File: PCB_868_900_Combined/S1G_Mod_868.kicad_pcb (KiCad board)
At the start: 4 copper layers, 60 x 27 mm, 89 parts, among them J2 20021121-00010C4LF, J5 0475890001-MicroUSBPort, P1 61301621121, Q1 DMG2307L-7, SW1 CUS-12TB, SW2 B3U-1000P, T1 0732511150, U1 AP7361-33FGE-7, U2 ADF7023BCPZ, U3 STM32L052C8T6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

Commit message: Readme
Readme updated and boms exported.
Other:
- board text added: "PWR"
- board text removed: "CERN OSHWL 1.2 Nov 2016"
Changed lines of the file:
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@@
     (links 234)
     (no_connects 0)
-    (area 39.924999 33.1276 120.075001 67.3654)
+    (area 56.424999 37.924999 116.575001 65.075001)
     (thickness 1.6)
     (drawings 15)
@@
   (layers
     (0 F.Cu signal)
-    (1 In1.Cu power hide)
-    (2 In2.Cu power hide)
-    (31 B.Cu signal hide)
+    (1 In1.Cu power)
+    (2 In2.Cu power)
+    (31 B.Cu signal)
     (32 B.Adhes user)
     (33 F.Adhes user)
@@
     (38 B.Mask user)
     (39 F.Mask user)
-    (40 Dwgs.User user)
+    (40 Dwgs.User user hide)
     (41 Cmts.User user)
     (42 Eco1.User user)
@@
       (drillshape 0)
       (scaleselection 1)
-      (outputdirectory ""))
+      (outputdirectory Fab_Outputs/))
   )
   (net 0 "")
@@
   (module PCB_Footprints:LED0603 (layer F.Cu)
     (at 105.425 50.6 180)
-    (fp_text reference LED4 (at -0.375 0.9 180) (layer F.SilkS)
+    (fp_text reference LED4 (at 1.675 -1.05 180) (layer F.SilkS)
       (effects (font (size 0.5 0.5) (thickness 0.1)))
     )
@@
     )
   )
+  (gr_text PWR (at 103.85 49.35) (layer F.SilkS)
+    (effects (font (size 1 1) (thickness 0.15)) (justify left))
+  )
   (gr_text RST (at 86.8 45.3 90) (layer F.SilkS)
     (effects (font (size 1 1) (thickness 0.15)) (justify left))
@@
     (effects (font (size 1 1) (thickness 0.18)) (justify left mirror))
   )
-  (gr_text "CERN OSHWL 1.2 Nov 2016" (at 61.9 63.6) (layer F.SilkS)
-    (effects (font (size 1 1) (thickness 0.15)) (justify left))
-  )
   (gr_line (start 40 51.5) (end 120 51.5) (layer Dwgs.User) (width 0.15))
   (gr_text "S1G-RF 01.a - 915MHZ Radio\n" (at 62.3 39.6) (layer F.SilkS)
@@
   (segment (start 99.14 49.75) (end 100.85 49.75) (width 0.1778) (layer F.Cu) (net 42))
   (segment (start 100.85 49.75) (end 101.3 49.3) (width 0.1778) (layer F.Cu) (net 42))
-  (segment (start 101.3 49.3) (end 101.3 44.4) (width 0.1778) (layer F.Cu) (net 42))
-  (segment (start 101.3 44.4) (end 100.94 44.04) (width 0.1778) (layer F.Cu) (net 42))
-  (segment (start 100.94 44.04) (end 99.33 44.04) (width 0.1778) (layer F.Cu) (net 42))
+  (segment (start 101.3 49.3) (end 101.3 44.5) (width 0.1778) (layer F.Cu) (net 42))
+  (segment (start 101.3 44.5) (end 100.84 44.04) (width 0.1778) (layer F.Cu) (net 42))
+  (segment (start 100.84 44.04) (end 99.33 44.04) (width 0.1778) (layer F.Cu) (net 42))
   (segment (start 99.53 44.04) (end 100.66 44.04) (width 0.1778) (layer F.Cu) (net 42))
   (segment (start 99.14 50.75) (end 101.99 50.75) (width 0.1778) (layer F.Cu) (net 44))
@@
   (segment (start 94.14 46.573) (end 93.55 45.983) (width 0.1778) (layer F.Cu) (net 54))
   (segment (start 93.54 45.993) (end 93.55 45.983) (width 0.1778) (layer F.Cu) (net 54))
-  (segment (start 99.33 42.77) (end 100.355 42.77) (width 0.1778) (layer F.Cu) (net 59))
-  (segment (start 100.355 42.77) (end 101.7 44.115) (width 0.1778) (layer F.Cu) (net 59))
-  (segment (start 101.7 44.115) (end 101.7 46.800012) (width 0.1778) (layer F.Cu) (net 59))
+  (segment (start 99.33 42.77) (end 100.22 42.77) (width 0.1778) (layer F.Cu) (net 59))
+  (segment (start 100.22 42.77) (end 101.7 44.25) (width 0.1778) (layer F.Cu) (net 59))
+  (segment (start 101.7 44.25) (end 101.7 46.800012) (width 0.1778) (layer F.Cu) (net 59))
   (segment (start 101.7 46.800012) (end 102.099988 47.2) (width 0.1778) (layer F.Cu) (net 59))
   (segment (start 98.3 47.2) (end 102.099988 47.2) (width 0.1778) (layer B.Cu) (net 59))

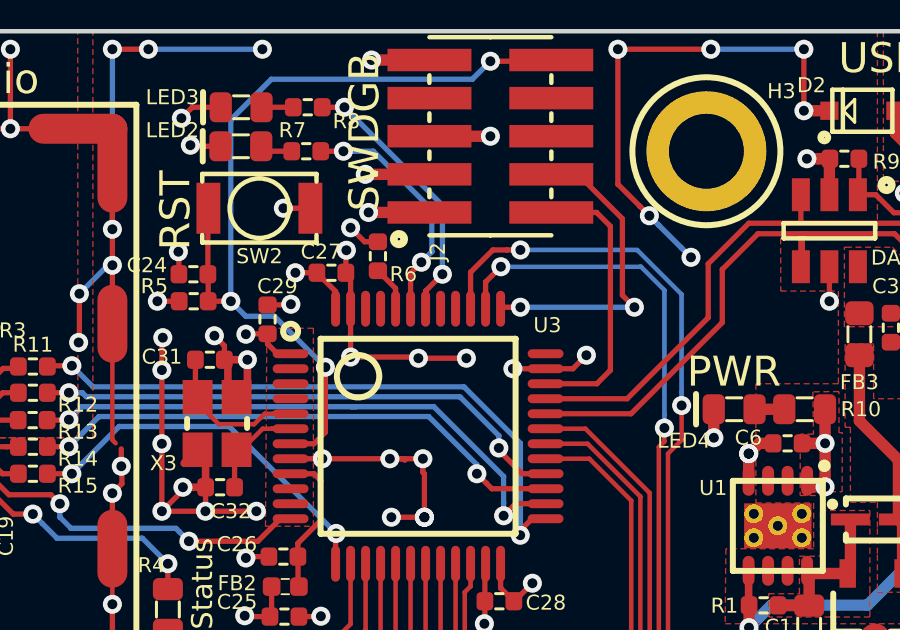
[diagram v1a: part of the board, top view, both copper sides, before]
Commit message: USB VDD
Found schematic bug, USB VDD was not tied to 3V3 supply or applied a
bypass cap, this has been resolved in both implementations of the S1G.
STM32L0 program manual added to the datasheets collection for the
project. Schematic PDFs updated.
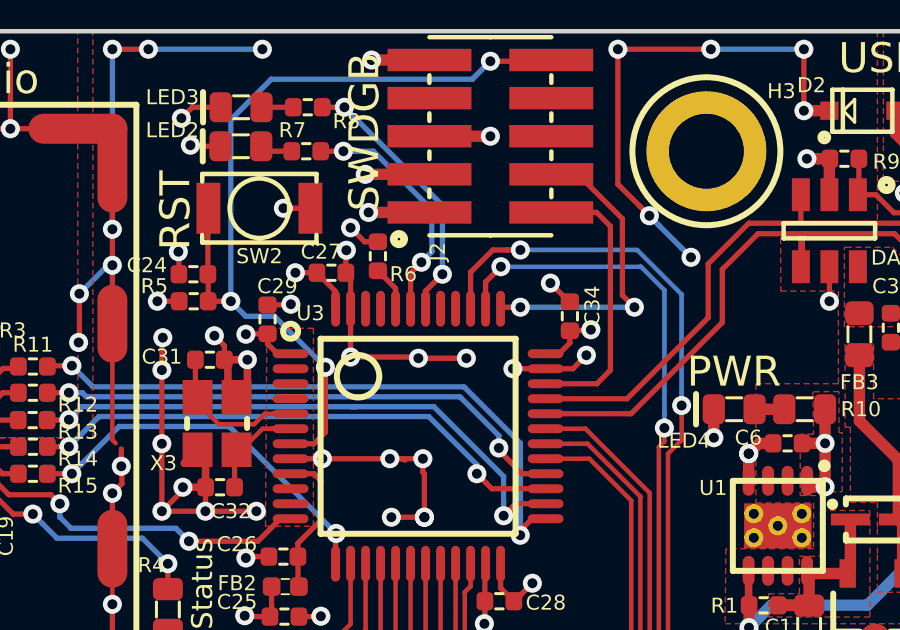
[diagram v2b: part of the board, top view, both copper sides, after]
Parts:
- added C34: CL05B104JP5NNNC, PCB_Footprints:C0402, F.Cu at (100.0, 47.5)
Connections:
- U3 pad 36: Net-(U3-Pad36) -> +3V3
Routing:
- net +3V3: track 24.3 -> 26.4 mm, vias 12 -> 13
- net GND: track 373.3 -> 374.2 mm, vias 174 -> 175

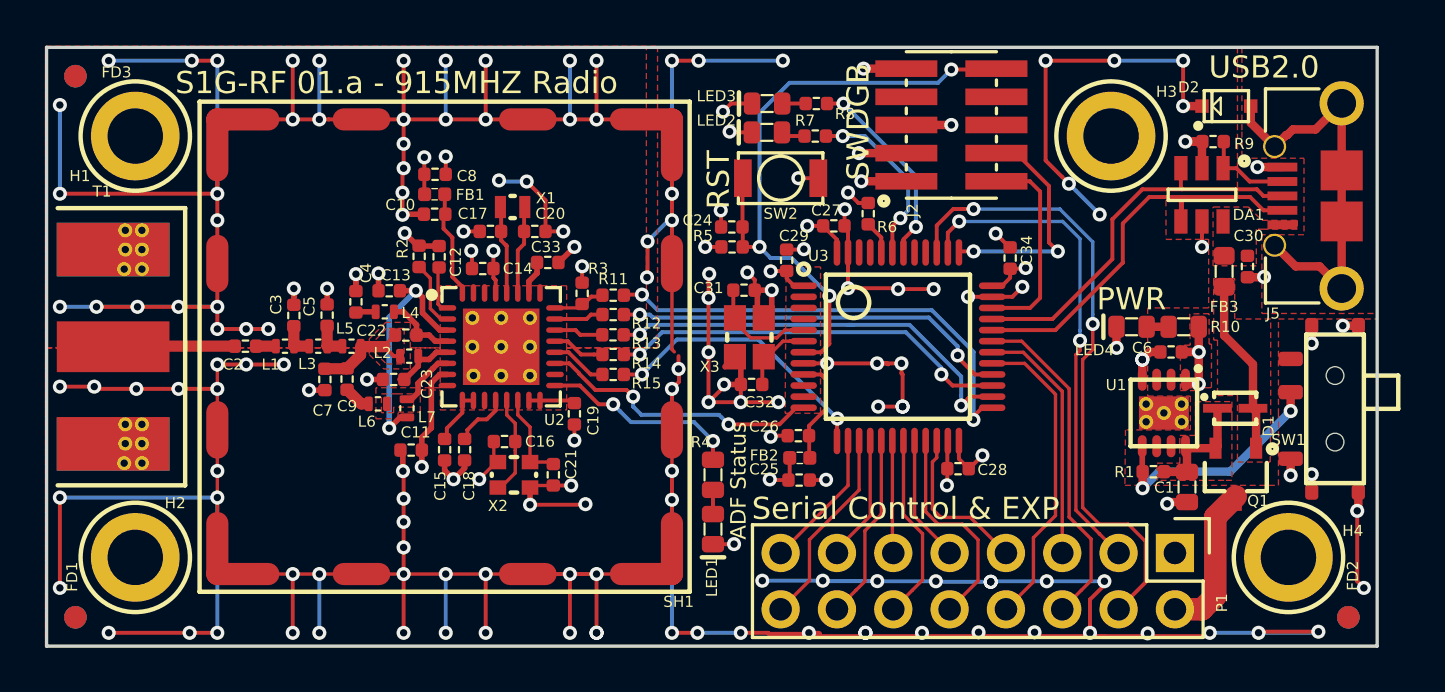
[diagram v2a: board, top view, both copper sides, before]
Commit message: 0.22uF cap
0.22uF cap replaced with 0402 part instead of the massive 0603 part.
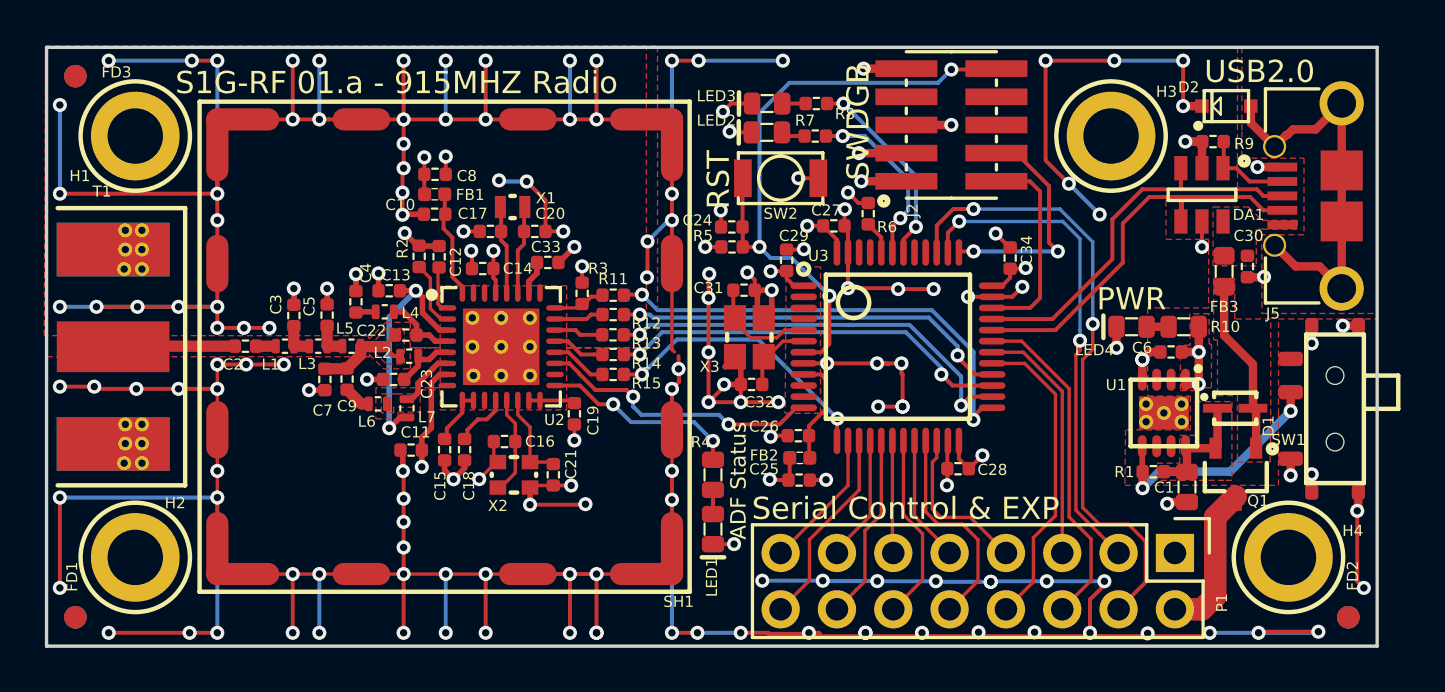
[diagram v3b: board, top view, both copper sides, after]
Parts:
- C12, C13, C15, C19, C33: value CL10B224JO8NNNC -> CL05A224KP5NNNC
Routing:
- net Net-(C22-Pad1): track 4.80 -> 5.95 mm

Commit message: Radio Reference Schematic Errors
Some errors transcribing ADI's reference shcematic. 0.22uF caps added to
pins that needed it etc.
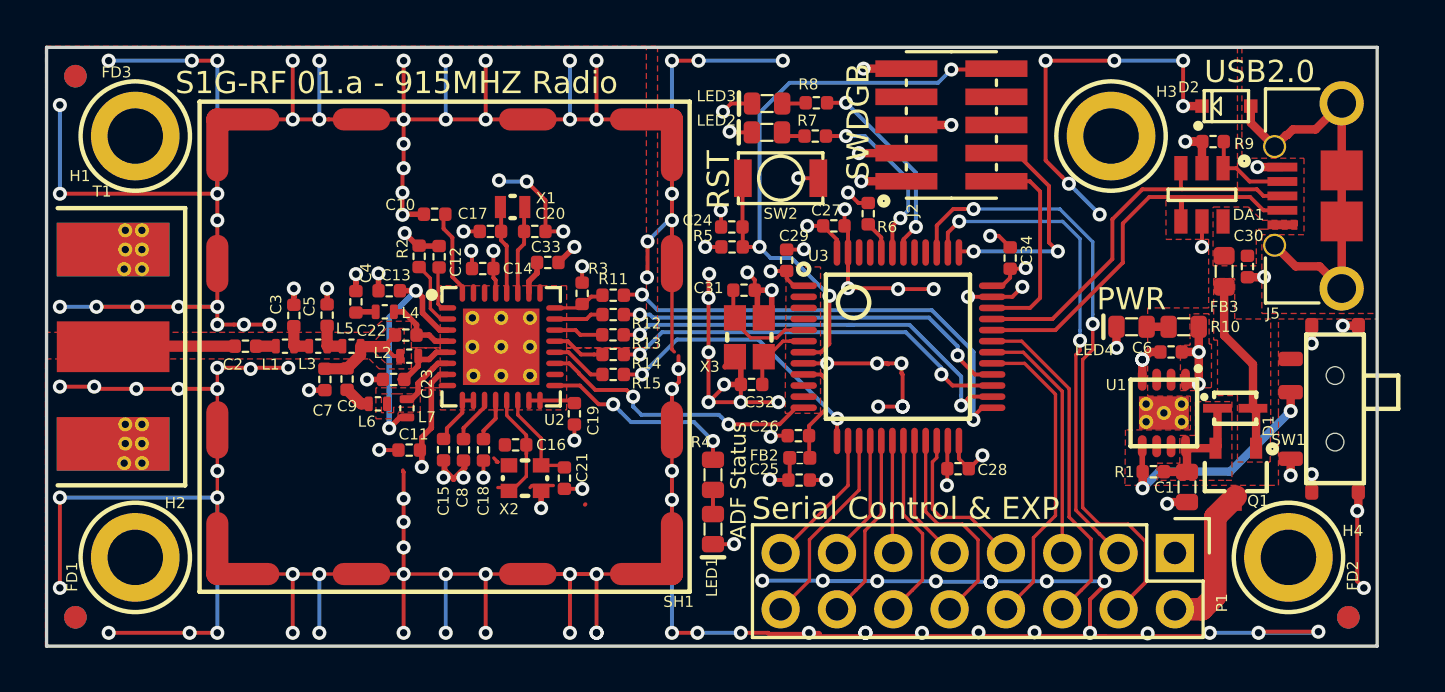
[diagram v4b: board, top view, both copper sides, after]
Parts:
- removed FB1: BLM15HG601SN1D, PCB_Footprints:BLM15HG601SN1D
- C10, C8: value CL05B104JP5NNNC -> CL05A224KP5NNNC
- moved C8 12.5 mm to (75.3, 56.1), turned to 270 degrees
- moved C18 0.85 mm to (76.2, 56.1)
- moved C16 0.52 mm to (77.7, 55.9)
- moved C21 0.52 mm to (79.8, 57.4)
- moved X2 0.52 mm to (78.1, 57.4)
- moved C11 0.09 mm to (72.8, 56.2)
- turned R8 to 180 degrees
- turned R7 to 180 degrees
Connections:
- net /VREF renamed Net-(C10-Pad2)
- C8 pad 1: GND -> Net-(C8-Pad1)
- C8 pad 2: +3V3 -> GND
- R7 pad 1: Net-(LED2-Pad1) -> /MCU - STM32L052K8T6/HB_2
- R7 pad 2: Net-(R7-Pad2) -> Net-(LED2-Pad1)
- R8 pad 1: Net-(LED3-Pad1) -> /MCU - STM32L052K8T6/HB_1
- R8 pad 2: Net-(R8-Pad2) -> Net-(LED3-Pad1)
- U2 pad 11: Net-(U2-Pad11) -> Net-(C8-Pad1)
- U3 pad 42: Net-(R8-Pad2) -> /MCU - STM32L052K8T6/HB_1
- U3 pad 43: Net-(R7-Pad2) -> /MCU - STM32L052K8T6/HB_2
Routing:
- net /MCU - STM32L052K8T6/HB_1: track 0.00 -> 9.14 mm, vias 0 -> 2
- net Net-(R8-Pad2): track 9.04 -> 0.00 mm, vias 2 -> 0
- net Net-(R7-Pad2): track 8.11 -> 0.00 mm, vias 2 -> 0
- net /MCU - STM32L052K8T6/HB_2: track 0.00 -> 8.11 mm, vias 0 -> 2
- net GND: track 374.4 -> 370.9 mm, vias 175 -> 174
- net Net-(C8-Pad1): track 0.00 -> 2.14 mm
- net +3V3: track 26.4 -> 24.7 mm, vias 13 -> 12
- net (no net): track 0.00 -> 1.45 mm
- net Net-(C10-Pad2): track 4.92 -> 3.98 mm

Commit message: PDF
schematic exported as color PDF for review
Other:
- board text added: "Hackaday Prize 2017 - adamjvr"
- board text added: "S1G RF 01.a - 915MHZ Radio CERN OSHW 1.2 July 2017 Designed by Adam Vadala-Roth https://github.com/adamjvr/S1G-Mod"
- board text removed: "S1G RF 01.a - 915MHZ Radio CERN OSHW 1.2 Nov 2016 Designed by Adam Vadala-Roth https://github.com/adamjvr/S1G-Mod"
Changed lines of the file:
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@@
     (area 39.924999 24.75 146.100001 67.3654)
     (thickness 1.6)
-    (drawings 17)
+    (drawings 18)
     (tracks 993)
     (zones 0)
@@
     (34 B.Paste user)
     (35 F.Paste user)
-    (36 B.SilkS user hide)
+    (36 B.SilkS user)
     (37 F.SilkS user)
     (38 B.Mask user)
@@
   (module PCB_Footprints:36103205 locked (layer F.Cu)
     (at 74.45 51.5)
-    (fp_text reference SH1 (at 10.55 11.5) (layer F.SilkS)
+    (fp_text reference SH1 (at -11.5 -7.55 90) (layer F.SilkS)
       (effects (font (size 0.5 0.5) (thickness 0.1)))
     )
@@
     )
   )
+  (gr_text "Hackaday Prize 2017 - adamjvr " (at 62.15 63.45) (layer F.SilkS)
+    (effects (font (size 1 1) (thickness 0.18)) (justify left))
+  )
   (dimension 60 (width 0.3) (layer Eco1.User)
     (gr_text "60.000 mm" (at 86.5 26.1) (layer Eco1.User)
@@
     (effects (font (size 1 1) (thickness 0.15)) (justify left))
   )
-  (gr_text "S1G RF 01.a - 915MHZ Radio\nCERN OSHW 1.2 Nov 2016\nDesigned by Adam Vadala-Roth\nhttps://github.com/adamjvr/S1G-Mod\n\n" (at 87.2 43.3) (layer B.SilkS)
+  (gr_text "S1G RF 01.a - 915MHZ Radio\nCERN OSHW 1.2 July 2017\nDesigned by Adam Vadala-Roth\nhttps://github.com/adamjvr/S1G-Mod\n\n" (at 87.2 43.3) (layer B.SilkS)
     (effects (font (size 1 1) (thickness 0.18)) (justify left mirror))
   )
